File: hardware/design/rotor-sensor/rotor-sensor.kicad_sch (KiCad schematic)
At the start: 89 parts, among them J2 Conn_01x06, J517 Conn_ARM_JTAG_SWD_10, U1 MCP2021A-500E/SN, U2 AP22804AW5, U5 AP22804AW5, U500 ATSAMD21E18A-A, U501 AP2127K-ADJTRG1, Y508 ABS07-32.768KHZ-7-T

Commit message: Finalizing hardware design
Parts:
- added FID1, FID2: Fiducial, Fiducial:Fiducial_0.5mm_Mask1mm, symbol Mechanical:Fiducial
- added R505 (x2): 10k, Resistor_SMD:R_0402_1005Metric, symbol Device:R
- C1, C3: Rating (none) -> 25V; Size (none) -> 0805
- C2: Rating (none) -> 25V; Size (none) -> 0603
- C21, C22, C23, C24, C25, C4, C5, C6, C7, R1, R10, R11, R17, R18, R19, R2, R20, R3, R5, R6, R7, R8, R9: Size (none) -> 0402
- C513: Size 0805 -> 1206
- D706: now not fitted
- R4: SIze (none) -> 0603
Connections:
- net +5V: now also R505.1, R505.1
- net at R11.2, U5.3 (~{FLG}): now also R505.2
- net at R8.2, U2.3 (~{FLG}): now also R505.2
- net M04_EN1/~{SLEEP}/DIAG renamed M04_~{SLEEP}/DIAG/EN1
- net M04_INPUT1 renamed M04_INPUT1/~{ERR}/INPUT1
- net M04_INPUT1_DIAG renamed M04_INPUT1_DIAG/OE/~{FLAG}
- net M04_INPUT2 renamed M04_INPUT2/INPUT2/INPUT2
- net M04_INPUT2_DIAG/INPUT2 renamed M04_INPUT2_DIAG/INPUT1/~{FLAG}
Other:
- note added: "Mechanical & Assembly"
- moved on the sheet: C512, R516, TP605

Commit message: Fab. layer cleanup
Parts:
- U600: value ~ -> BMI088
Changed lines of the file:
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@@
       (effects (font (size 1.27 1.27)))
     )
-    (property "Value" "~" (at 212.09 80.01 0)
+    (property "Value" "BMI088" (at 212.09 80.01 0)
       (effects (font (size 1.27 1.27)))
     )

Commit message: Hardware design finalization
FIxing architecture diagram
Changes to PCB fab layer
Fixes DNF components in schematic
Increases document width
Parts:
- R1, R7: value 10k -> 4.7k
- R18, R19, R2, R3: now not fitted
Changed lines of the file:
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@@
   )
   (symbol (lib_id "Device:R") (at 323.215 99.06 90) (unit 1)
-    (in_bom yes) (on_board yes) (dnp no)
+    (in_bom yes) (on_board yes) (dnp yes)
     (property "Reference" "R2" (at 321.31 96.52 90)
       (effects (font (size 1.27 1.27)))
@@
   )
   (symbol (lib_id "Device:R") (at 318.135 64.77 180) (unit 1)
-    (in_bom yes) (on_board yes) (dnp no)
+    (in_bom yes) (on_board yes) (dnp yes)
     (property "Reference" "R18" (at 319.913 63.3105 0)
       (effects (font (size 1.27 1.27)) (justify right))
@@
       (effects (font (size 1.27 1.27)) (justify right))
     )
-    (property "Value" "10k" (at 262.89 157.48 0)
+    (property "Value" "4.7k" (at 262.89 157.48 0)
       (effects (font (size 1.27 1.27)) (justify right))
     )
@@
   )
   (symbol (lib_id "Device:R") (at 318.135 104.14 180) (unit 1)
-    (in_bom yes) (on_board yes) (dnp no)
+    (in_bom yes) (on_board yes) (dnp yes)
     (property "Reference" "R3" (at 319.913 103.4963 0)
       (effects (font (size 1.27 1.27)) (justify right))
@@
       (effects (font (size 1.27 1.27)) (justify right))
     )
-    (property "Value" "10k" (at 269.875 157.48 0)
+    (property "Value" "4.7k" (at 269.875 157.48 0)
       (effects (font (size 1.27 1.27)) (justify right))
     )
@@
   )
   (symbol (lib_id "Device:R") (at 323.215 59.69 90) (unit 1)
-    (in_bom yes) (on_board yes) (dnp no)
+    (in_bom yes) (on_board yes) (dnp yes)
     (property "Reference" "R19" (at 320.675 57.15 90)
       (effects (font (size 1.27 1.27)))

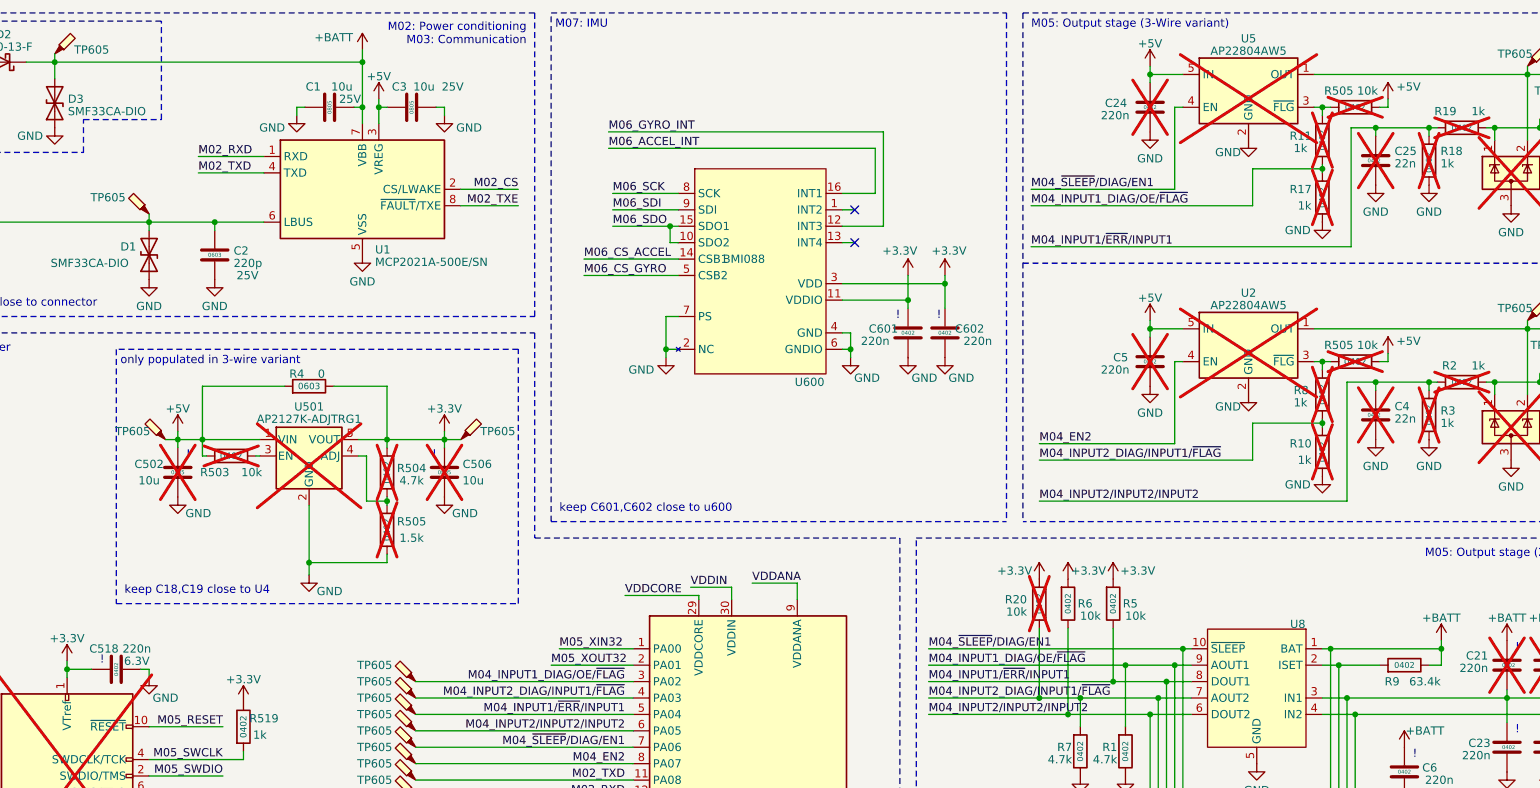
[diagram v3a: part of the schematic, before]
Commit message: Hardware Gen2 design freeze (#14)
* Fix label in connector schematic and added JWPF 3 pin connector
* Optical sensor adapter & CI workflow changes
* 5V rail renamed to VCC
* Fixed size information on some resistors
* Added Hall sensor position on PCB
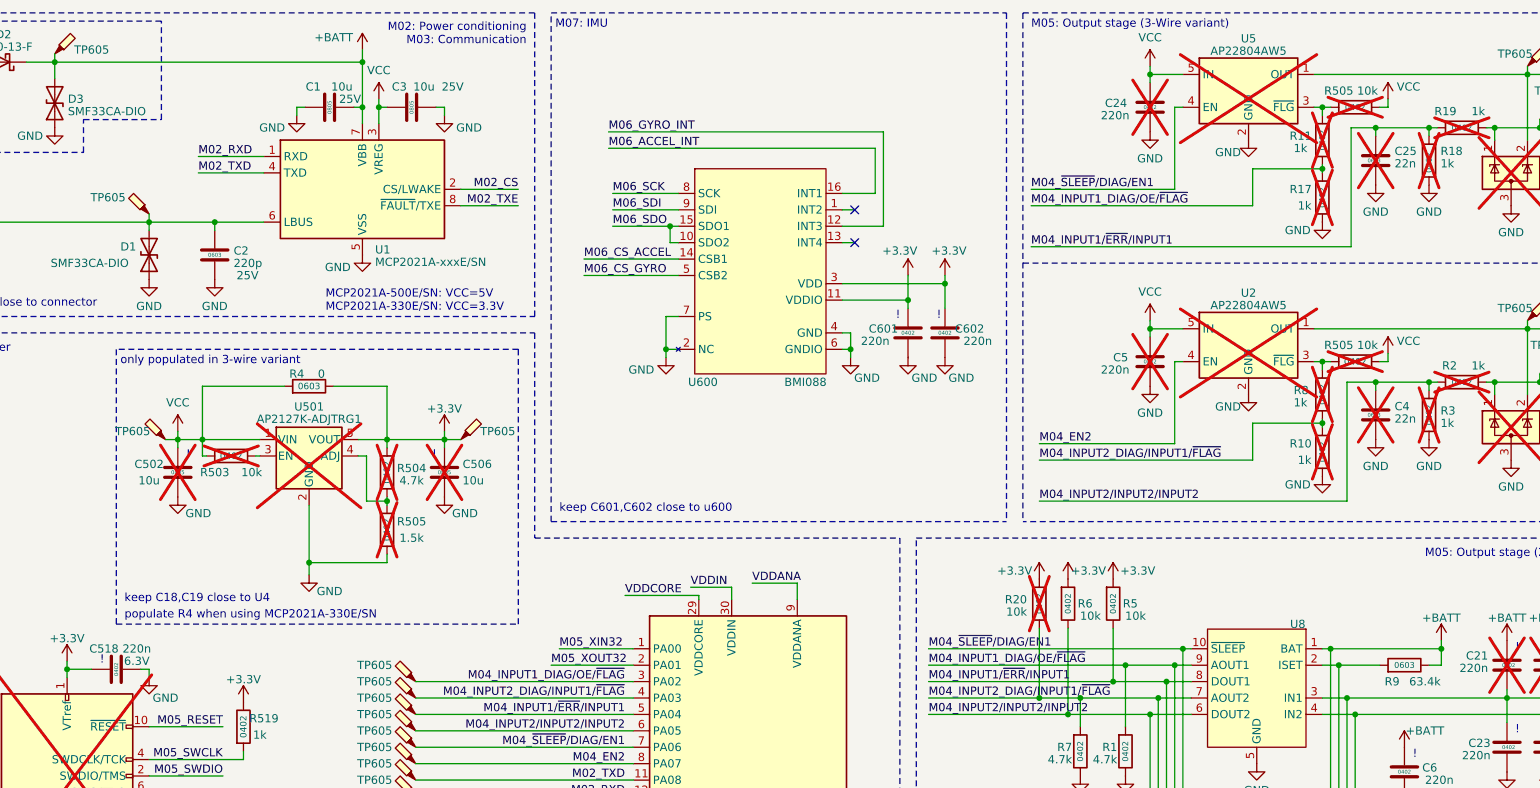
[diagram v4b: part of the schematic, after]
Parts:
- C25, C4, R9: Size 0402 -> 0603
- R4: SIze 0603 -> (none); Size (none) -> 0603
- U1: value MCP2021A-500E/SN -> MCP2021A-xxxE/SN
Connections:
- net +5V renamed VCC
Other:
- note added: "MCP2021A-500E/SN: VCC=5V MCP2021A-330E/SN: VCC=3.3V"
- note added: "populate R4 when using MCP2021A-330E/SN"

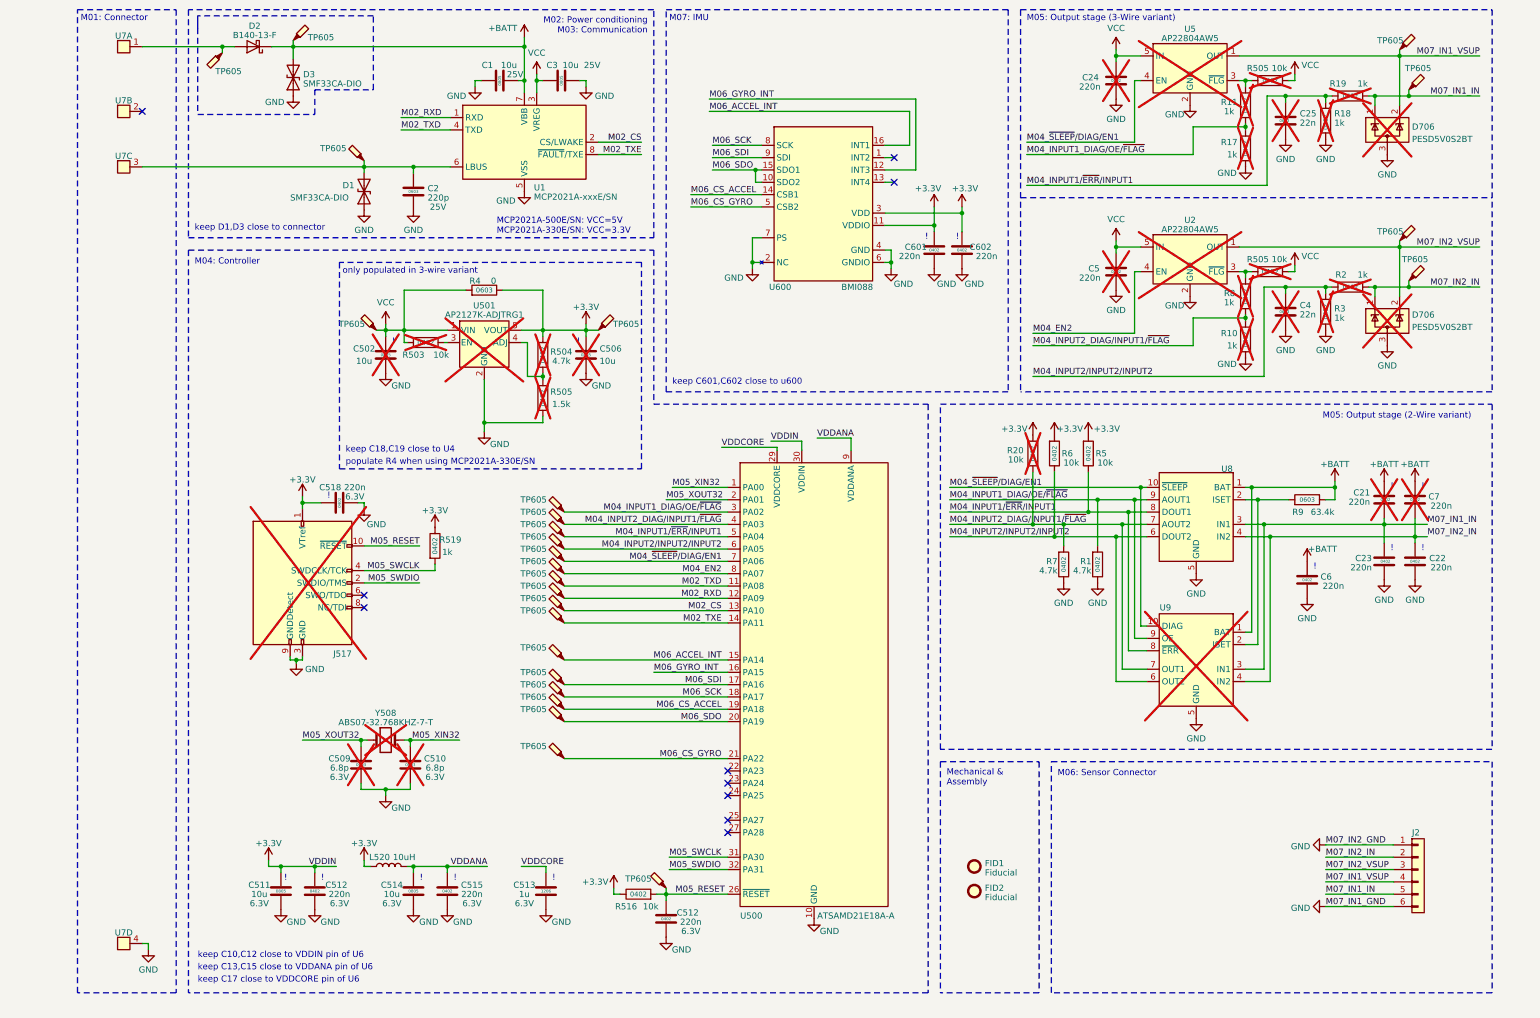
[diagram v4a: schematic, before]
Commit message: New schematic done
Works with TLIN1028-Q1 transceiver
Added BMP581 pressure sensor
Removed 3wire output stage
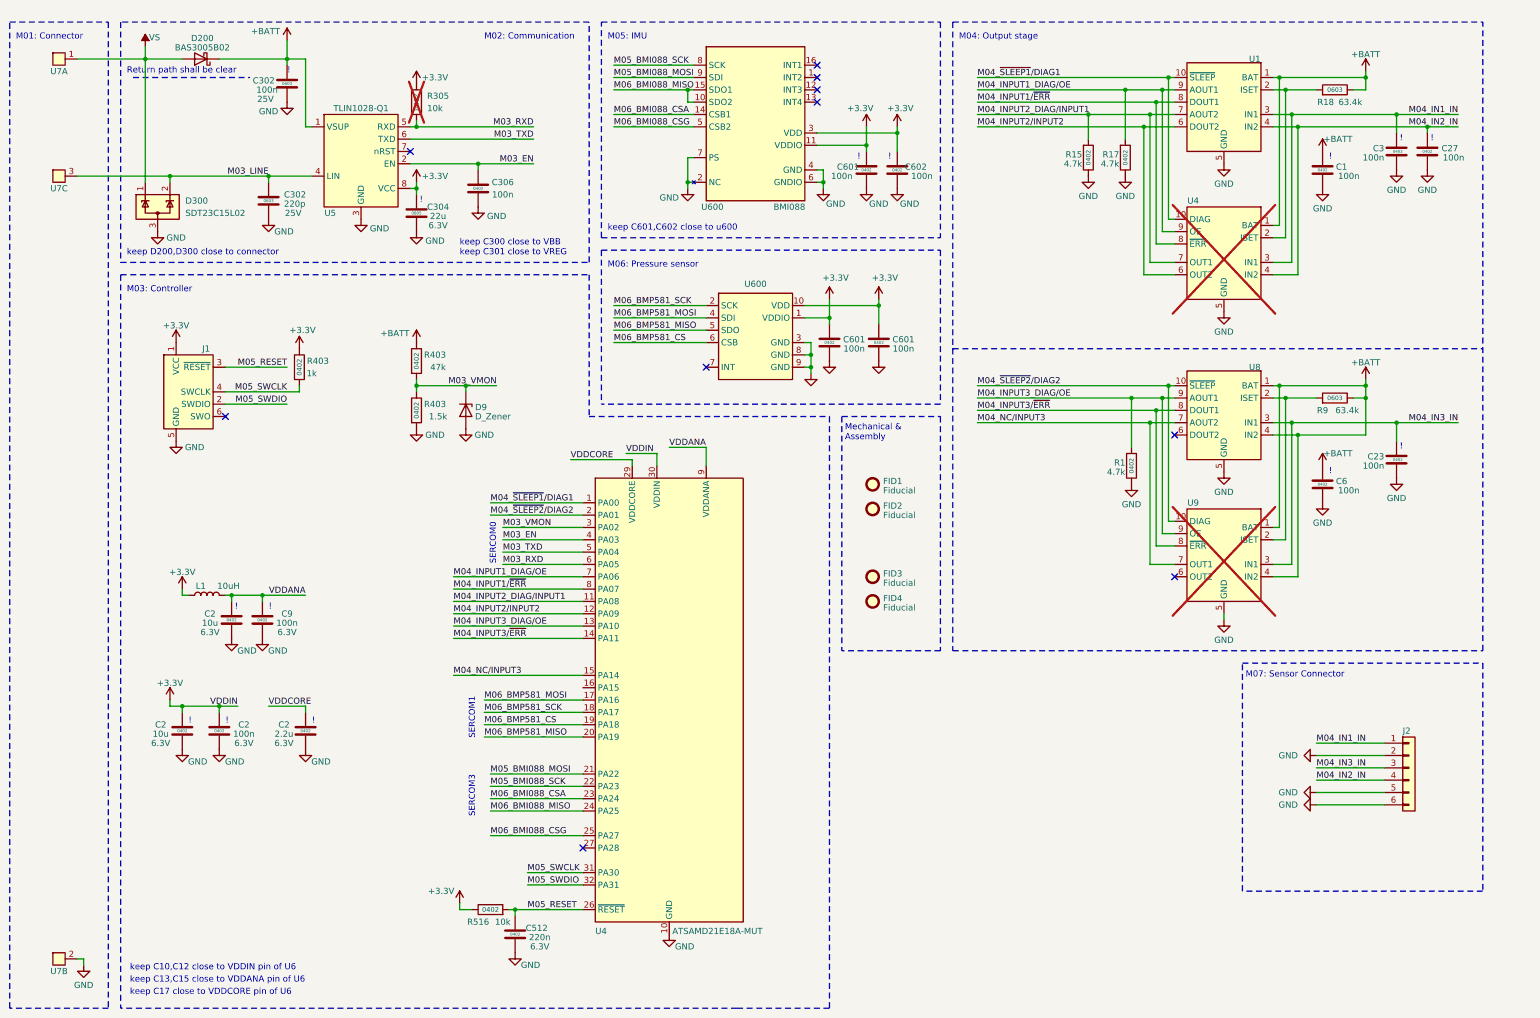
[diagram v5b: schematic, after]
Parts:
- removed C2: 220p, Capacitor_SMD:C_0603_1608Metric, symbol Device:C
- removed C21, C22, C24, C5, C512, C515, C518, C7: 220n, Capacitor_SMD:C_0402_1005Metric, symbol Device:C
- removed C25, C4: 22n, Capacitor_SMD:C_0603_1608Metric, symbol Device:C
- removed C502, C506, C511, C514: 10u, Capacitor_SMD:C_0805_2012Metric, symbol Device:C
- removed C509, C510: 6.8p, Capacitor_SMD:C_0603_1608Metric, symbol Device:C
- removed C513: 1u, Capacitor_SMD:C_1206_3216Metric, symbol Device:C
- removed D1, D3: SMF33CA-DIO, Diode_SMD:D_SMF, symbol Device:D_TVS
- removed D2: B140-13-F, Diode_SMD:D_SMA, symbol Device:D_Schottky
- removed D706 (x2): PESD5V0S2BT, Package_TO_SOT_SMD:SOT-23, symbol Power_Protection:SP0502BAHT
- removed J517: Conn_ARM_JTAG_SWD_10, Connector_PinHeader_1.27mm:PinHeader_2x05_P1.27mm_Vertical_SMD, symbol Connector:Conn_ARM_JTAG_SWD_10
- removed L520: 10uH, Inductor_SMD:L_0805_2012Metric, symbol Device:L
- removed R10, R11, R19, R2, R3, R519, R8: 1k, Resistor_SMD:R_0402_1005Metric, symbol Device:R
- removed R20, R5, R503, R505 (x2), R6: 10k, Resistor_SMD:R_0402_1005Metric, symbol Device:R
- removed R4: 0, Resistor_SMD:R_0603_1608Metric, symbol Device:R
- removed R504, R7: 4.7k, Resistor_SMD:R_0402_1005Metric, symbol Device:R
- removed R505: 1.5k, Resistor_SMD:R_0402_1005Metric, symbol Device:R
- removed TP605: O4, TestPoint:TestPoint_Pad_1.0x1.0mm, symbol Connector:TestPoint_Probe
- removed TP605: P1, TestPoint:TestPoint_Pad_1.0x1.0mm, symbol Connector:TestPoint_Probe
- removed TP605: O6, TestPoint:TestPoint_Pad_1.0x1.0mm, symbol Connector:TestPoint_Probe
- removed TP605: M1, TestPoint:TestPoint_Pad_1.0x1.0mm, symbol Connector:TestPoint_Probe
- removed TP605: S4, TestPoint:TestPoint_Pad_1.0x1.0mm, symbol Connector:TestPoint_Probe
- removed TP605: B1, TestPoint:TestPoint_Pad_1.0x1.0mm, symbol Connector:TestPoint_Probe
- removed TP605: O3, TestPoint:TestPoint_Pad_1.0x1.0mm, symbol Connector:TestPoint_Probe
- removed TP605: V1, TestPoint:TestPoint_Pad_1.0x1.0mm, symbol Connector:TestPoint_Probe
- removed TP605: O7, TestPoint:TestPoint_Pad_1.0x1.0mm, symbol Connector:TestPoint_Probe
- removed TP605: O8, TestPoint:TestPoint_Pad_1.0x1.0mm, symbol Connector:TestPoint_Probe
- removed TP605: O2, TestPoint:TestPoint_Pad_1.0x1.0mm, symbol Connector:TestPoint_Probe
- removed TP605: S7, TestPoint:TestPoint_Pad_1.0x1.0mm, symbol Connector:TestPoint_Probe
- removed TP605: S1, TestPoint:TestPoint_Pad_1.0x1.0mm, symbol Connector:TestPoint_Probe
- removed TP605: B3, TestPoint:TestPoint_Pad_1.0x1.0mm, symbol Connector:TestPoint_Probe
- removed TP605: O10, TestPoint:TestPoint_Pad_1.0x1.0mm, symbol Connector:TestPoint_Probe
- removed TP605: S6, TestPoint:TestPoint_Pad_1.0x1.0mm, symbol Connector:TestPoint_Probe
- removed TP605: P2, TestPoint:TestPoint_Pad_1.0x1.0mm, symbol Connector:TestPoint_Probe
- removed TP605: O5, TestPoint:TestPoint_Pad_1.0x1.0mm, symbol Connector:TestPoint_Probe
- removed TP605: S5, TestPoint:TestPoint_Pad_1.0x1.0mm, symbol Connector:TestPoint_Probe
- removed TP605: B2, TestPoint:TestPoint_Pad_1.0x1.0mm, symbol Connector:TestPoint_Probe
- removed TP605: B5, TestPoint:TestPoint_Pad_1.0x1.0mm, symbol Connector:TestPoint_Probe
- removed TP605: S3, TestPoint:TestPoint_Pad_1.0x1.0mm, symbol Connector:TestPoint_Probe
- removed TP605: B4, TestPoint:TestPoint_Pad_1.0x1.0mm, symbol Connector:TestPoint_Probe
- removed TP605: O1, TestPoint:TestPoint_Pad_1.0x1.0mm, symbol Connector:TestPoint_Probe
- removed TP605: V2, TestPoint:TestPoint_Pad_1.0x1.0mm, symbol Connector:TestPoint_Probe
- removed TP605: O9, TestPoint:TestPoint_Pad_1.0x1.0mm, symbol Connector:TestPoint_Probe
- removed U1: MCP2021A-xxxE/SN, Package_SO:SOIC-8_3.9x4.9mm_P1.27mm, symbol Interface_CAN_LIN:MCP2021A-xxxxSN
- removed U2, U5: AP22804AW5, Package_TO_SOT_SMD:SOT-23-5, symbol Power_Management:AP22804AW5
- removed U500: ATSAMD21E18A-A, Package_QFP:TQFP-32_7x7mm_P0.8mm, symbol MCU_Microchip_SAMD:ATSAMD21E18A-A
- removed U501: AP2127K-ADJTRG1, Package_TO_SOT_SMD:SOT-23-5, symbol Regulator_Linear:AP2127K-ADJ
- removed unit 4 of U7
- removed Y508: ABS07-32.768KHZ-7-T, Crystal:Crystal_SMD_3215-2Pin_3.2x1.5mm, symbol Device:Crystal
- added C2 (x2): 10u, Capacitor_SMD:C_0402_1005Metric, symbol Device:C
- added C2, C27, C306, C601 (x2), C9: 100n, Capacitor_SMD:C_0402_1005Metric, symbol Device:C
- added C2: 2.2u, Capacitor_SMD:C_0402_1005Metric, symbol Device:C
- added C302: 100n, Capacitor_SMD:C_0603_1608Metric, symbol Device:C
- added C302: 220p, Capacitor_SMD:C_0603_1608Metric, symbol Device:C
- added C304: 22u, Capacitor_SMD:C_0805_2012Metric, symbol Device:C
- added D200: BAS3005B02, Diode_SMD:D_SOD-523, symbol Device:D_Schottky
- added D300: SDT23C15L02, Package_TO_SOT_SMD:SOT-23, symbol Power_Protection:SP0502BAHT
- added D9: D_Zener, Diode_SMD:D_SOD-523, symbol Device:D_Zener
- added FID3, FID4: Fiducial, Fiducial:Fiducial_0.5mm_Mask1mm, symbol Mechanical:Fiducial
- added J1: Conn_ARM_SWD_TagConnect_TC2030-NL, Connector:Tag-Connect_TC2030-IDC-NL_2x03_P1.27mm_Vertical, symbol Connector:Conn_ARM_SWD_TagConnect_TC2030-NL
- added L1: 10uH, Inductor_SMD:L_0603_1608Metric, symbol Device:L
- added R15: 4.7k, Resistor_SMD:R_0402_1005Metric, symbol Device:R
- added R305: 10k, Resistor_SMD:R_0402_1005Metric, symbol Device:R
- added R403: 1.5k, Resistor_SMD:R_0402_1005Metric, symbol Device:R
- added R403: 1k, Resistor_SMD:R_0402_1005Metric, symbol Device:R
- added R403: 47k, Resistor_SMD:R_0402_1005Metric, symbol Device:R
- added U1: ~, Package_SO:MSOP-10_3x3mm_P0.5mm, symbol local_symbols:MAX9621
- added U4: ATSAMD21E18A-MUT, Package_DFN_QFN:VQFN-32-1EP_5x5mm_P0.5mm_EP3.5x3.5mm, symbol MCU_Microchip_SAMD:ATSAMD21E18A-A
- added U4: ~, Package_SO:MSOP-10_3x3mm_P0.5mm, symbol local_symbols:MAX9921
- added U5: TLIN1028-Q1, Package_SON:Texas_S-PVSON-N8, symbol local_symbols:TLIN1028-Q1
- added U600: ~, local_footprints:Bosch_LGA10, symbol local_symbols:BMP581
- C1, C3: value 10u -> 100n; footprint Capacitor_SMD:C_0805_2012Metric -> Capacitor_SMD:C_0402_1005Metric; Rating 25V -> (none); Size 0805 -> 0402
- C23, C6, C601, C602: value 220n -> 100n
- J2: footprint local_footprints:SMD_6PIN -> local_footprints:SOIC-6
- R17: value 1k -> 4.7k; now fitted
- R18: value 1k -> 63.4k; footprint Resistor_SMD:R_0402_1005Metric -> Resistor_SMD:R_0603_1608Metric; Size 0402 -> 0603; now fitted
- U7: footprint local_footprints:SMD_4PIN -> local_footprints:SOIC-4
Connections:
- net M07_IN2_VSUP is gone; now on net M04_IN3_IN: J2.3 (Pin_3)
- net VCC is gone; now on net GND: C3.1
- net +3.3V: now also C2.2, C2.2, C304.1, C601.2, C601.2, J1.1 (VCC), L1.1, R305.1, R403.1, U4.30 (VDDIN), U5.8 (VCC), U600.1 (VDDIO), U600.10 (VDD)
- net +BATT: now also R18.1, U8.4 (IN2), U9.4 (IN2), C302.2, D200.1 (K), R403.1, U1.1 (BAT), U4.1 (BAT), U5.1 (VSUP)
- net GND: now also J2.2 (Pin_2), J2.5 (Pin_5), U7.2, C2.1, C2.1, C2.1, C2.1, C27.1, C302.1, C302.2, C304.2, C306.1, C601.1, C601.1, C9.1, D300.3 (A), D9.2 (A), J1.5 (GND), R15.1, R403.2, U1.5 (GND), U4.10 (GND), U4.28 (GND), U4.5 (GND), U5.3 (GND), U600.3 (GND), U600.8 (GND), U600.9 (GND); no longer C3.2, J2.1 (Pin_1), R18.1
- net M05_RESET: now also J1.3 (~{RESET}), U4.26 (~{RESET})
- net M05_SWCLK: now also J1.4 (SWCLK), R403.2, U4.31 (PA30)
- net M05_SWDIO: now also J1.2 (SWDIO), U4.32 (PA31)
- net VDDANA: now also C2.2, C9.2, L1.2, U4.9 (VDDANA)
- net VDDCORE: now also C2.2, U4.29 (VDDCORE)
- net M03_LINE: now reaches U7.3
- net M03_LINE: now also C302.1, D300.2 (K), U5.4 (LIN)
- net VS: now reaches U7.1
- net VS: now also D200.2 (A), D300.1 (K)
- net M04_INPUT1_DIAG/OE/~{FLAG} renamed M04_INPUT3_DIAG/OE
- net M04_INPUT3_DIAG/OE: now also U4.13 (PA10); no longer R17.2
- net M04_INPUT1/~{ERR}/INPUT1 renamed M04_INPUT3/~{ERR}
- net M04_INPUT3/~{ERR}: now also U4.14 (PA11); no longer R18.2
- net M04_INPUT2_DIAG/INPUT1/~{FLAG} renamed M04_NC/INPUT3
- net M04_NC/INPUT3: now also U4.15 (PA14)
- net M04_INPUT2/INPUT2/INPUT2: no longer names the net of U9.6 (OUT2)
- net M04_INPUT2/INPUT2/INPUT2: no longer U8.6 (DOUT2)
- net M04_~{SLEEP}/DIAG/EN1 renamed M04_~{SLEEP2}/DIAG2
- net M04_~{SLEEP2}/DIAG2: now also U4.2 (PA01)
- net M06_ACCEL_INT: no longer names the net of U600.16 (INT1)
- net M06_CS_ACCEL renamed M06_BMI088_CSA
- net M06_BMI088_CSA: now also U4.23 (PA24)
- net M06_CS_GYRO renamed M06_BMI088_CSG
- net M06_BMI088_CSG: now also U4.25 (PA27)
- net M06_GYRO_INT: no longer names the net of U600.12 (INT3)
- net M06_SCK renamed M05_BMI088_SCK
- net M05_BMI088_SCK: now also U4.22 (PA23)
- net M06_SDI renamed M05_BMI088_MOSI
- net M05_BMI088_MOSI: now also U4.21 (PA22)
- net M06_SDO renamed M06_BMI088_MISO
- net M06_BMI088_MISO: now also U4.24 (PA25)
- net M07_IN1_IN renamed M04_IN3_IN
- net M04_IN3_IN: no longer J2.5 (Pin_5)
- net M07_IN1_VSUP renamed M04_IN2_IN
- net M04_IN2_IN: now also C27.2, U1.4 (IN2), U4.4 (IN2)
- removed net M07_IN2_IN: J2.2 (Pin_2), U8.4 (IN2), U9.4 (IN2)
- new net: R18.2, U1.2 (ISET), U4.2 (ISET)
- new net M03_EN: C306.2, U4.4 (PA03), U5.2 (EN)
- new net M03_RXD: R305.2, U4.6 (PA05), U5.5 (RXD)
- new net M03_TXD: U4.5 (PA04), U5.6 (TXD)
- new net M03_VMON: D9.1 (K), R403.1, R403.2, U4.3 (PA02)
- new net M04_IN1_IN: C3.2, J2.1 (Pin_1), U1.3 (IN1), U4.3 (IN1)
- new net M04_INPUT1_DIAG/OE: R17.2, U1.9 (AOUT1), U4.7 (PA06), U4.9 (OE)
- new net M04_INPUT1/~{ERR}: U1.8 (DOUT1), U4.8 (PA07), U4.8 (~{ERR})
- new net M04_INPUT2_DIAG/INPUT1: R15.2, U1.7 (AOUT2), U4.11 (PA08), U4.7 (OUT1)
- new net M04_INPUT2/INPUT2: U1.6 (DOUT2), U4.12 (PA09), U4.6 (OUT2)
- new net M04_~{SLEEP1}/DIAG1: U1.10 (~{SLEEP}), U4.1 (PA00), U4.10 (DIAG)
- new net M06_BMP581_CS: U4.19 (PA18), U600.6 (CSB)
- new net M06_BMP581_MISO: U4.20 (PA19), U600.5 (SDO)
- new net M06_BMP581_MOSI: U4.17 (PA16), U600.4 (SDI)
- new net M06_BMP581_SCK: U4.18 (PA17), U600.2 (SCK)
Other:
- note added: "M02: Communication"
- note added: "M03: Controller"
- note added: "M04: Output stage"
- note added: "M05: IMU"
- note added: "M06: Pressure sensor"
- note added: "M07: Sensor Connector"
- note added: "Return path shall be clear"
- note added: "SERCOM0"
- note added: "SERCOM1"
- note added: "SERCOM3"
- note added: "keep C300 close to VBB keep C301 close to VREG"
- note added: "keep D200,D300 close to connector"
- note removed: "M02: Power conditioning M03: Communication"
- note removed: "M04: Controller"
- note removed: "M05: Output stage (2-Wire variant)"
- note removed: "M05: Output stage (3-Wire variant)"
- note removed: "M06: Sensor Connector"
- note removed: "M07: IMU"
- note removed: "MCP2021A-500E/SN: VCC=5V MCP2021A-330E/SN: VCC=3.3V"
- note removed: "keep C18,C19 close to U4"
- note removed: "keep D1,D3 close to connector"
- note removed: "only populated in 3-wire variant"
- note removed: "populate R4 when using MCP2021A-330E/SN"
- moved on the sheet: C23, C512, C6, C601, C602, FID1, FID2, J2, R1, R516, R9, U600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
